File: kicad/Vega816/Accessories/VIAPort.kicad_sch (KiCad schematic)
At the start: 5 parts, among them J107 VIA Port, J108 16B, U129 W65C22SxP

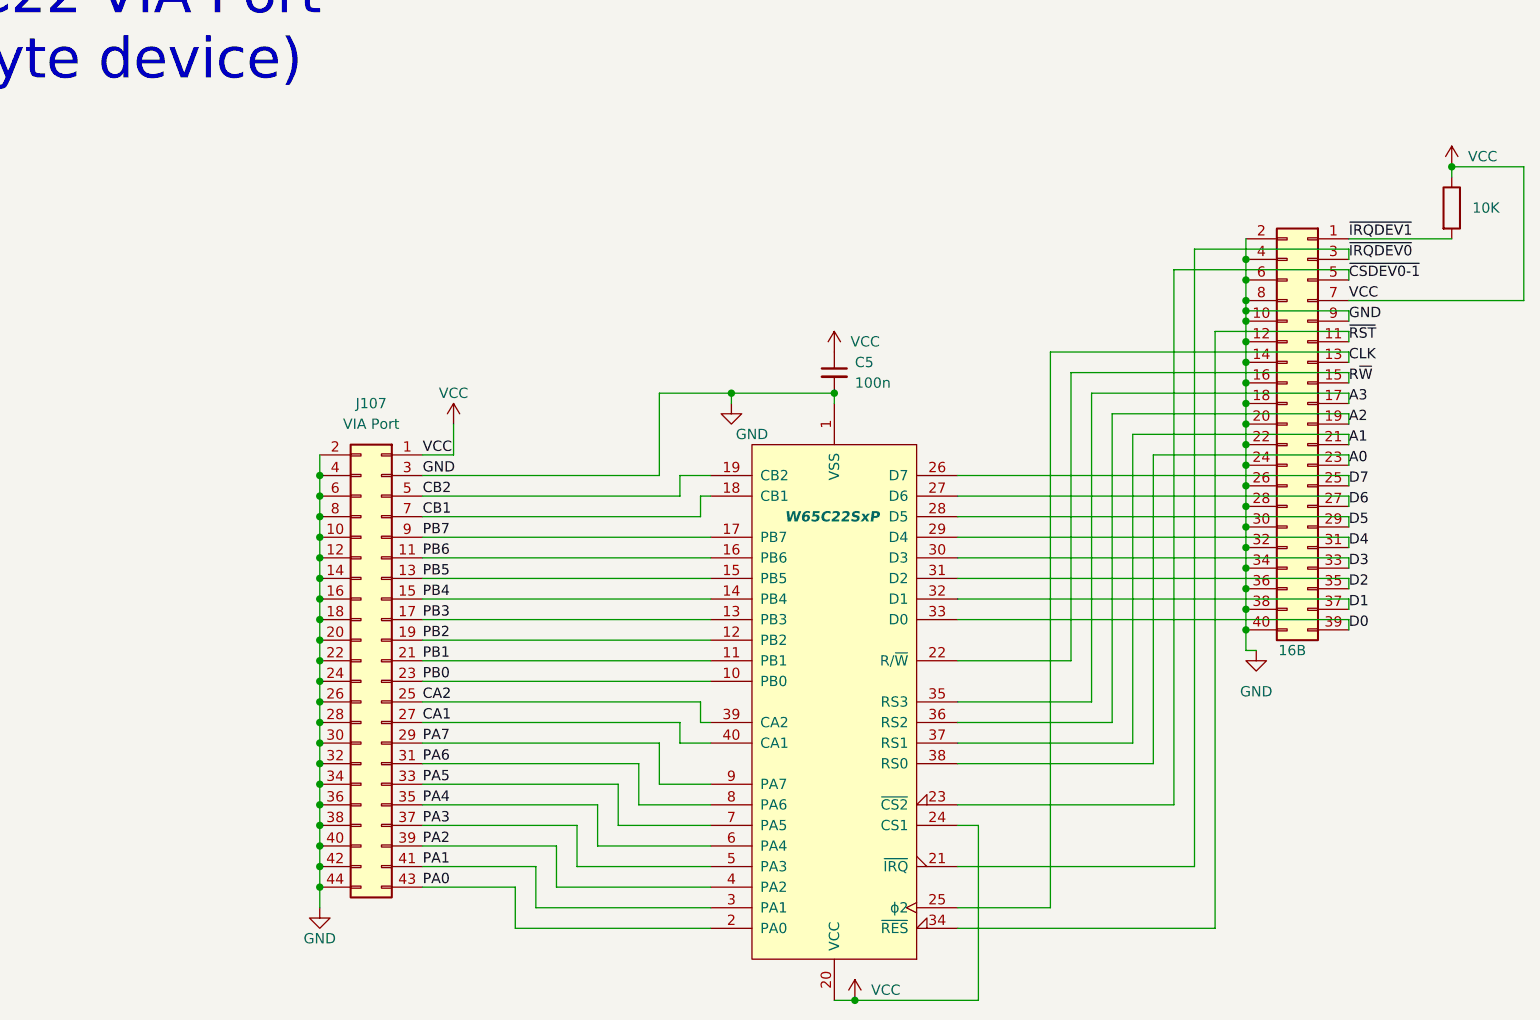
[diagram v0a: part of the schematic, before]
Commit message: via port rework
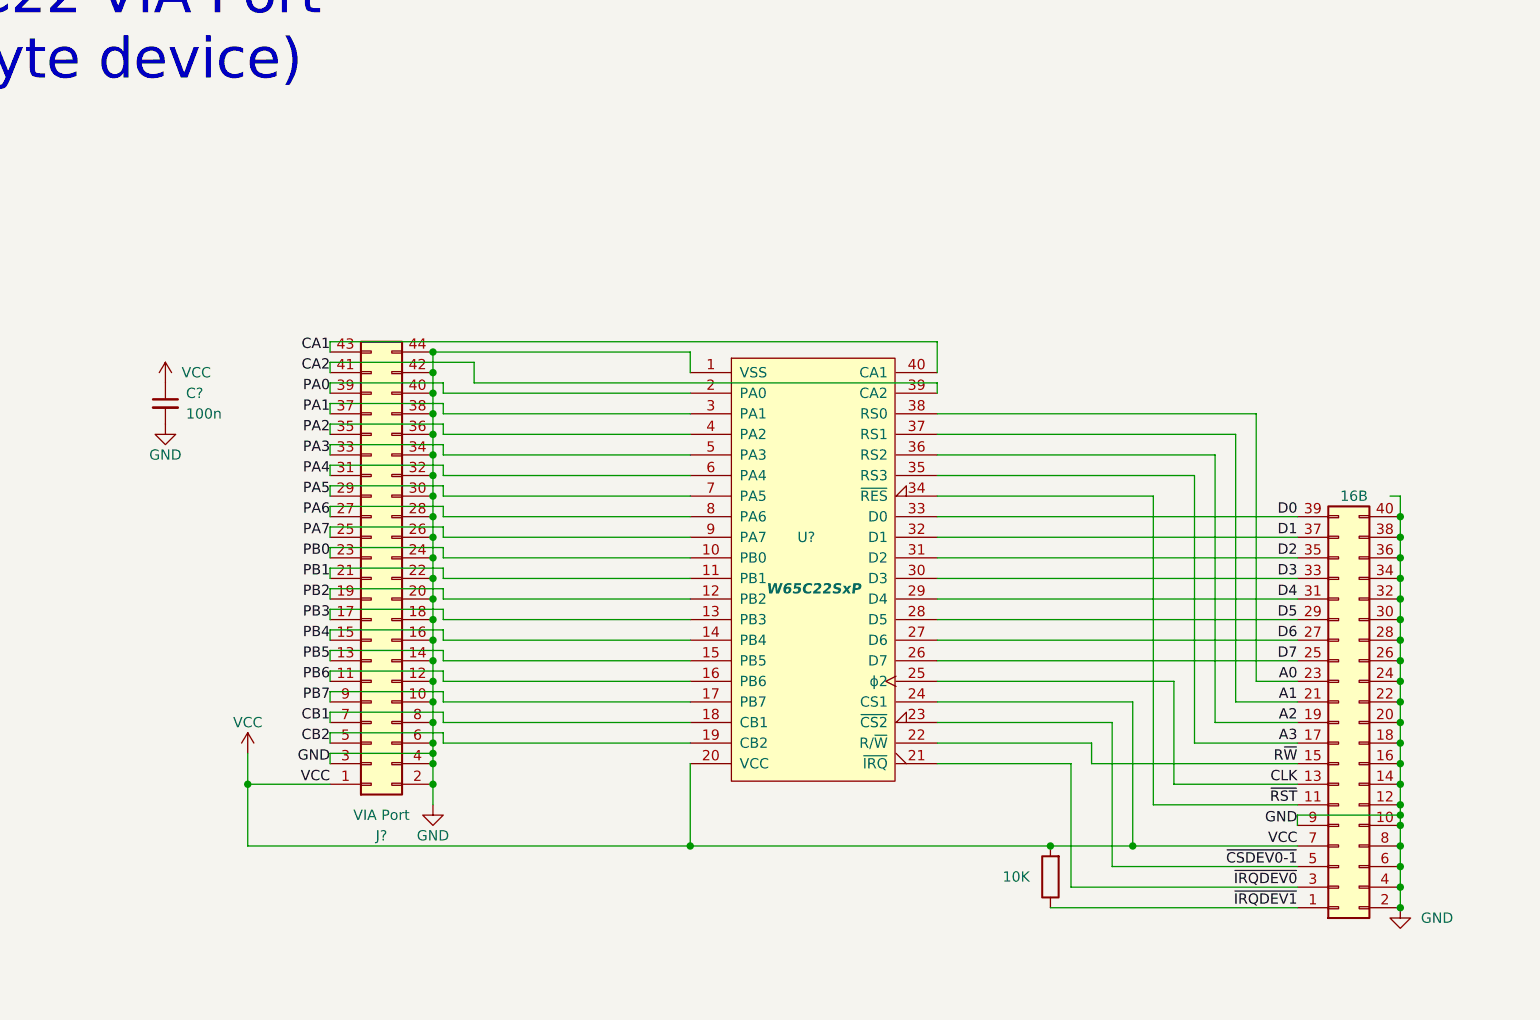
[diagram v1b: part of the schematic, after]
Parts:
- removed C5: 100n, symbol Device:C_Small
- removed J107: VIA Port, symbol Connector_Generic:Conn_02x22_Odd_Even
- removed J108: 16B, symbol Connector_Generic:Conn_02x20_Odd_Even
- removed R16: 10K, symbol Device:R
- removed U129: W65C22SxP, Package_DIP:DIP-40_W15.24mm_Socket, symbol 65C816:W65C22SxP
- added C?: 100n, symbol Device:C_Small
- added J?: 16B, symbol Connector_Generic:Conn_02x20_Odd_Even
- added J?: VIA Port, symbol Connector_Generic:Conn_02x22_Odd_Even
- added R?: 10K, symbol Device:R
- added U?: W65C22SxP, Package_DIP:DIP-40_W15.24mm_Socket, symbol Vega816:W65C22SxP
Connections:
- net A0: now also J?.23 (Pin_23), U?.38 (RS0)
- net A1: now also J?.21 (Pin_21), U?.37 (RS1)
- net A2: now also J?.19 (Pin_19), U?.36 (RS2)
- net A3: now also J?.17 (Pin_17), U?.35 (RS3)
- net CA1: now also J?.43 (Pin_43), U?.40 (CA1)
- net CA2: now also J?.41 (Pin_41), U?.39 (CA2)
- net CB1: now also J?.7 (Pin_7), U?.18 (CB1)
- net CB2: now also J?.5 (Pin_5), U?.19 (CB2)
- net CLK: now also J?.13 (Pin_13), U?.25 (ϕ2)
- net D0: now also J?.39 (Pin_39), U?.33 (D0)
- net D1: now also J?.37 (Pin_37), U?.32 (D1)
- net D2: now also J?.35 (Pin_35), U?.31 (D2)
- net D3: now also J?.33 (Pin_33), U?.30 (D3)
- net D4: now also J?.31 (Pin_31), U?.29 (D4)
- net D5: now also J?.29 (Pin_29), U?.28 (D5)
- net D6: now also J?.27 (Pin_27), U?.27 (D6)
- net D7: now also J?.25 (Pin_25), U?.26 (D7)
- net GND: now also C?.2, J?.10 (Pin_10), J?.10 (Pin_10), J?.12 (Pin_12), J?.12 (Pin_12), J?.14 (Pin_14), J?.14 (Pin_14), J?.16 (Pin_16), J?.16 (Pin_16), J?.18 (Pin_18), J?.18 (Pin_18), J?.2 (Pin_2), J?.2 (Pin_2), J?.20 (Pin_20), J?.20 (Pin_20), J?.22 (Pin_22), J?.22 (Pin_22), J?.24 (Pin_24), J?.24 (Pin_24), J?.26 (Pin_26), J?.26 (Pin_26), J?.28 (Pin_28), J?.28 (Pin_28), J?.3 (Pin_3), J?.30 (Pin_30), J?.30 (Pin_30), J?.32 (Pin_32), J?.32 (Pin_32), J?.34 (Pin_34), J?.34 (Pin_34), J?.36 (Pin_36), J?.36 (Pin_36), J?.38 (Pin_38), J?.38 (Pin_38), J?.4 (Pin_4), J?.4 (Pin_4), J?.40 (Pin_40), J?.40 (Pin_40), J?.42 (Pin_42), J?.44 (Pin_44), J?.6 (Pin_6), J?.6 (Pin_6), J?.8 (Pin_8), J?.8 (Pin_8), J?.9 (Pin_9), U?.1 (VSS)
- net PA0: now also J?.39 (Pin_39), U?.2 (PA0)
- net PA1: now also J?.37 (Pin_37), U?.3 (PA1)
- net PA2: now also J?.35 (Pin_35), U?.4 (PA2)
- net PA3: now also J?.33 (Pin_33), U?.5 (PA3)
- net PA4: now also J?.31 (Pin_31), U?.6 (PA4)
- net PA5: now also J?.29 (Pin_29), U?.7 (PA5)
- net PA6: now also J?.27 (Pin_27), U?.8 (PA6)
- net PA7: now also J?.25 (Pin_25), U?.9 (PA7)
- net PB0: now also J?.23 (Pin_23), U?.10 (PB0)
- net PB1: now also J?.21 (Pin_21), U?.11 (PB1)
- net PB2: now also J?.19 (Pin_19), U?.12 (PB2)
- net PB3: now also J?.17 (Pin_17), U?.13 (PB3)
- net PB4: now also J?.15 (Pin_15), U?.14 (PB4)
- net PB5: now also J?.13 (Pin_13), U?.15 (PB5)
- net PB6: now also J?.11 (Pin_11), U?.16 (PB6)
- net PB7: now also J?.9 (Pin_9), U?.17 (PB7)
- net R~{W}: now also J?.15 (Pin_15), U?.22 (R/~{W})
- net VCC: now also C?.1, J?.1 (Pin_1), J?.7 (Pin_7), R?.2, U?.20 (VCC), U?.24 (CS1)
- net ~{CSDEV0-1}: now also J?.5 (Pin_5), U?.23 (~{CS2})
- net ~{IRQDEV0}: now also J?.3 (Pin_3), U?.21 (~{IRQ})
- net ~{IRQDEV1}: now also J?.1 (Pin_1), R?.1
- net ~{RST}: now also J?.11 (Pin_11), U?.34 (~{RES})

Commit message: Big
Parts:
- removed J?: 16B, symbol Connector_Generic:Conn_02x20_Odd_Even
- removed R?: 10K, symbol Device:R
- added C22, C23, C36, C37, C38, C39, C40, C41: 100n, symbol Device:C_Small
- added J21, J22: VIA Port, symbol Connector_Generic:Conn_02x22_Odd_Even
- added J25: ACIA0, symbol Connector_Generic:Conn_02x04_Odd_Even
- added J26: ACIA1, symbol Connector_Generic:Conn_02x04_Odd_Even
- added J27: ACIA2, symbol Connector_Generic:Conn_02x04_Odd_Even
- added J36: ACIA3, symbol Connector_Generic:Conn_02x04_Odd_Even
- added J?: I/O Port, symbol Connector_Generic:Conn_02x20_Odd_Even
- added U75, U76: W65C22SxP, Package_DIP:DIP-40_W15.24mm_Socket, symbol Vega816:W65C22SxP
- added U77, U80, U83, U86: W65C51NxP, symbol BB816:W65C51NxP
- added U81, U82: 74ACH138, Package_DIP:DIP-14_W7.62mm_Socket, symbol Vega816:74ACH138
- added X2: 1.8432MHz, Oscillator:Oscillator_DIP-8, symbol Oscillator:CXO_DIP8
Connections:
- net A0: now also J?.23 (Pin_23), U75.38 (RS0), U76.38 (RS0), U77.13 (RS0), U80.13 (RS0), U83.13 (RS0), U86.13 (RS0)
- net A1: now also J?.21 (Pin_21), U75.37 (RS1), U76.37 (RS1), U77.14 (RS1), U80.14 (RS1), U83.14 (RS1), U86.14 (RS1)
- net A2: now also J?.19 (Pin_19), U75.36 (RS2), U76.36 (RS2), U82.2 (A1)
- net A3: now also J?.17 (Pin_17), U75.35 (RS3), U76.35 (RS3), U82.3 (A2)
- net CA1: now also J21.43 (Pin_43), J22.43 (Pin_43), U75.40 (CA1), U76.40 (CA1)
- net CA2: now also J21.41 (Pin_41), J22.41 (Pin_41), U75.39 (CA2), U76.39 (CA2)
- net CB1: now also J21.7 (Pin_7), J22.7 (Pin_7), U75.18 (CB1), U76.18 (CB1)
- net CB2: now also J21.5 (Pin_5), J22.5 (Pin_5), U75.19 (CB2), U76.19 (CB2)
- net CLK: now also J?.7 (Pin_7), U75.25 (ϕ2), U76.25 (ϕ2), U77.27 (ϕ2), U80.27 (ϕ2), U83.27 (ϕ2), U86.4 (~{RES})
- net D0: now also J?.39 (Pin_39), U75.33 (D0), U76.33 (D0), U77.18 (D0), U80.18 (D0), U83.18 (D0), U86.18 (D0)
- net D1: now also J?.37 (Pin_37), U75.32 (D1), U76.32 (D1), U77.19 (D1), U80.19 (D1), U83.19 (D1), U86.19 (D1)
- net D2: now also J?.35 (Pin_35), U75.31 (D2), U76.31 (D2), U77.20 (D2), U80.20 (D2), U83.20 (D2), U86.20 (D2)
- net D3: now also J?.33 (Pin_33), U75.30 (D3), U76.30 (D3), U77.21 (D3), U80.21 (D3), U83.21 (D3), U86.21 (D3)
- net D4: now also J?.31 (Pin_31), U75.29 (D4), U76.29 (D4), U77.22 (D4), U80.22 (D4), U83.22 (D4), U86.22 (D4)
- net D5: now also J?.29 (Pin_29), U75.28 (D5), U76.28 (D5), U77.23 (D5), U80.23 (D5), U83.23 (D5), U86.23 (D5)
- net D6: now also J?.27 (Pin_27), U75.27 (D6), U76.27 (D6), U77.24 (D6), U80.24 (D6), U83.24 (D6), U86.24 (D6)
- net D7: now also J?.25 (Pin_25), U75.26 (D7), U76.26 (D7), U77.25 (D7), U80.25 (D7), U83.25 (D7), U86.25 (D7)
- net GND: now also C22.2, C23.2, C36.2, C37.2, C38.2, C39.2, C40.2, C41.2, J21.10 (Pin_10), J21.12 (Pin_12), J21.14 (Pin_14), J21.16 (Pin_16), J21.18 (Pin_18), J21.2 (Pin_2), J21.20 (Pin_20), J21.22 (Pin_22), J21.24 (Pin_24), J21.26 (Pin_26), J21.28 (Pin_28), J21.3 (Pin_3), J21.30 (Pin_30), J21.32 (Pin_32), J21.34 (Pin_34), J21.36 (Pin_36), J21.38 (Pin_38), J21.4 (Pin_4), J21.40 (Pin_40), J21.42 (Pin_42), J21.44 (Pin_44), J21.6 (Pin_6), J21.8 (Pin_8), J22.10 (Pin_10), J22.12 (Pin_12), J22.14 (Pin_14), J22.16 (Pin_16), J22.18 (Pin_18), J22.2 (Pin_2), J22.20 (Pin_20), J22.22 (Pin_22), J22.24 (Pin_24), J22.26 (Pin_26), J22.28 (Pin_28), J22.3 (Pin_3), J22.30 (Pin_30), J22.32 (Pin_32), J22.34 (Pin_34), J22.36 (Pin_36), J22.38 (Pin_38), J22.4 (Pin_4), J22.40 (Pin_40), J22.42 (Pin_42), J22.44 (Pin_44), J22.6 (Pin_6), J22.8 (Pin_8), J?.10 (Pin_10), J?.12 (Pin_12), J?.14 (Pin_14), J?.16 (Pin_16), J?.18 (Pin_18), J?.2 (Pin_2), J?.20 (Pin_20), J?.22 (Pin_22), J?.24 (Pin_24), J?.26 (Pin_26), J?.28 (Pin_28), J?.3 (Pin_3), J?.30 (Pin_30), J?.32 (Pin_32), J?.34 (Pin_34), J?.36 (Pin_36), J?.38 (Pin_38), J?.4 (Pin_4), J?.40 (Pin_40), J?.6 (Pin_6), J?.8 (Pin_8), U75.1 (VSS), U76.1 (VSS), U77.1 (VSS), U77.16 (~{DCD}), U77.17 (~{DSR}), U77.9 (~{CTS}), U80.1 (VSS), U80.16 (~{DCD}), U80.17 (~{DSR}), U80.9 (~{CTS}), U81.1 (A0), U81.5 (E2), U81.8 (GND), U82.1 (A0), U82.5 (E2), U82.8 (GND), U83.1 (VSS), U83.16 (~{DCD}), U83.17 (~{DSR}), U83.9 (~{CTS}), U86.1 (VSS), U86.16 (~{DCD}), U86.17 (~{DSR}), U86.9 (~{CTS}), X2.4 (GND)
- net PA0: now also J21.39 (Pin_39), J22.39 (Pin_39), U75.2 (PA0), U76.2 (PA0)
- net PA1: now also J21.37 (Pin_37), J22.37 (Pin_37), U75.3 (PA1), U76.3 (PA1)
- net PA2: now also J21.35 (Pin_35), J22.35 (Pin_35), U75.4 (PA2), U76.4 (PA2)
- net PA3: now also J21.33 (Pin_33), J22.33 (Pin_33), U75.5 (PA3), U76.5 (PA3)
- net PA4: now also J21.31 (Pin_31), J22.31 (Pin_31), U75.6 (PA4), U76.6 (PA4)
- net PA5: now also J21.29 (Pin_29), J22.29 (Pin_29), U75.7 (PA5), U76.7 (PA5)
- net PA6: now also J21.27 (Pin_27), J22.27 (Pin_27), U75.8 (PA6), U76.8 (PA6)
- net PA7: now also J21.25 (Pin_25), J22.25 (Pin_25), U75.9 (PA7), U76.9 (PA7)
- net PB0: now also J21.23 (Pin_23), J22.23 (Pin_23), U75.10 (PB0), U76.10 (PB0)
- net PB1: now also J21.21 (Pin_21), J22.21 (Pin_21), U75.11 (PB1), U76.11 (PB1)
- net PB2: now also J21.19 (Pin_19), J22.19 (Pin_19), U75.12 (PB2), U76.12 (PB2)
- net PB3: now also J21.17 (Pin_17), J22.17 (Pin_17), U75.13 (PB3), U76.13 (PB3)
- net PB4: now also J21.15 (Pin_15), J22.15 (Pin_15), U75.14 (PB4), U76.14 (PB4)
- net PB5: now also J21.13 (Pin_13), J22.13 (Pin_13), U75.15 (PB5), U76.15 (PB5)
- net PB6: now also J21.11 (Pin_11), J22.11 (Pin_11), U75.16 (PB6), U76.16 (PB6)
- net PB7: now also J21.9 (Pin_9), J22.9 (Pin_9), U75.17 (PB7), U76.17 (PB7)
- net R~{W}: now also J?.9 (Pin_9), U75.22 (R/~{W}), U76.22 (R/~{W}), U77.28 (R/~{W}), U80.28 (R/~{W}), U83.28 (R/~{W}), U86.28 (R/~{W})
- net VCC: now also C22.1, C23.1, C36.1, C37.1, C38.1, C39.1, C40.1, C41.1, J21.1 (Pin_1), J22.1 (Pin_1), J25.1 (Pin_1), J26.1 (Pin_1), J27.1 (Pin_1), J36.1 (Pin_1), J?.1 (Pin_1), U75.20 (VCC), U75.24 (CS1), U76.20 (VCC), U76.24 (CS1), U77.15 (VCC), U77.2 (CS1), U80.15 (VCC), U80.2 (CS1), U81.16 (VCC), U81.6 (E3), U82.16 (VCC), U82.6 (E3), U83.15 (VCC), U83.2 (CS1), U86.15 (VCC), U86.2 (CS1), X2.1 (EN), X2.8 (Vcc)
- net ~{RST}: now also J?.5 (Pin_5), U75.34 (~{RES}), U76.34 (~{RES})
- net ~{CSDEV0-1}: no longer names the net of U?.23 (~{CS2})
- net ~{CSDEV0-1}: now also U81.15 (O0)
- net ~{IRQDEV0}: no longer names the net of U?.21 (~{IRQ})
- new net: J36.3 (Pin_3), U86.10 (TxD)
- new net: J36.5 (Pin_5), U86.12 (RxD)
- new net: U82.9 (O6), U86.3 (~{CS2})
- new net: U77.6 (XTAL1), U80.6 (XTAL1), U83.6 (XTAL1), U86.6 (XTAL1), X2.5 (OUT)
- new net: U75.23 (~{CS2}), U81.13 (O2)
- new net: J25.3 (Pin_3), U77.10 (TxD)
- new net: J25.5 (Pin_5), U77.12 (RxD)
- new net: U77.3 (~{CS2}), U82.15 (O0)
- new net: J36.2 (Pin_2), J36.4 (Pin_4), J36.6 (Pin_6), J36.7 (Pin_7), J36.8 (Pin_8)
- new net: J26.3 (Pin_3), U80.10 (TxD)
- new net: J26.5 (Pin_5), U80.12 (RxD)
- new net: U80.3 (~{CS2}), U82.13 (O2)
- new net: U82.11 (O4), U83.3 (~{CS2})
- new net: U81.9 (O6), U82.4 (E1)
- new net: U76.23 (~{CS2}), U81.11 (O4)
- new net: J26.2 (Pin_2), J26.4 (Pin_4), J26.6 (Pin_6), J26.7 (Pin_7), J26.8 (Pin_8)
- new net: J25.2 (Pin_2), J25.4 (Pin_4), J25.6 (Pin_6), J25.7 (Pin_7), J25.8 (Pin_8)
- new net: J27.2 (Pin_2), J27.4 (Pin_4), J27.6 (Pin_6), J27.7 (Pin_7), J27.8 (Pin_8)
- new net: J27.3 (Pin_3), U83.10 (TxD)
- new net: J27.5 (Pin_5), U83.12 (RxD)
- new net A4: J?.15 (Pin_15), U81.2 (A1)
- new net A5: J?.13 (Pin_13), U81.3 (A2)
- new net ~{CS}: J?.11 (Pin_11), U81.4 (E1)
- no-connect marks 0 -> 28
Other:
- note added: "System I/O 3 x VIA + 4 x ACIA"
- note removed: "W65C22 VIA Port (16 byte device)"
- moved on the sheet: C?, J?, U?

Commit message: dfsg
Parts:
- removed C22, C23, C36, C37, C38, C39, C40, C41, C?: 100n, symbol Device:C_Small
- removed J21, J22, J?: VIA Port, symbol Connector_Generic:Conn_02x22_Odd_Even
- removed J25: ACIA0, symbol Connector_Generic:Conn_02x04_Odd_Even
- removed J26: ACIA1, symbol Connector_Generic:Conn_02x04_Odd_Even
- removed J27: ACIA2, symbol Connector_Generic:Conn_02x04_Odd_Even
- removed J36: ACIA3, symbol Connector_Generic:Conn_02x04_Odd_Even
- removed J?: I/O Port, symbol Connector_Generic:Conn_02x20_Odd_Even
- removed U75, U76, U?: W65C22SxP, Package_DIP:DIP-40_W15.24mm_Socket, symbol Vega816:W65C22SxP
- removed U77, U80, U83, U86: W65C51NxP, symbol BB816:W65C51NxP
- removed U81, U82: 74ACH138, Package_DIP:DIP-14_W7.62mm_Socket, symbol Vega816:74ACH138
- removed X2: 1.8432MHz, Oscillator:Oscillator_DIP-8, symbol Oscillator:CXO_DIP8
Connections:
- no-connect marks 28 -> 0
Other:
- note removed: "System I/O 3 x VIA + 4 x ACIA"
